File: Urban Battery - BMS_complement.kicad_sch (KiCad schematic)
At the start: 41 parts, among them J1 BMS IO, J10 E-Stop, J11 Contactor Connector, J12 Thermistor, J13 Thermistor, J14 Thermistor, J2 OLED Header, J3 CAN, J4 CAN, J5 Charge Connector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

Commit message: updated component datasheets
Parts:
- U1: value MCP2515-xSO -> MCP2515-I/SO
- U2: value MCP2551-I-SN -> MCP2561/2
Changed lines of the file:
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@@
       (effects (font (size 1.27 1.27)) (justify left))
     )
-    (property "Value" "MCP2551-I-SN" (id 1) (at 132.8294 212.09 0)
+    (property "Value" "MCP2561/2" (id 1) (at 132.8294 212.09 0)
       (effects (font (size 1.27 1.27)) (justify left))
     )
@@
       (effects (font (size 1.27 1.27) italic) hide)
     )
-    (property "Datasheet" "http://ww1.microchip.com/downloads/en/devicedoc/21667d.pdf" (id 3) (at 130.81 222.25 0)
+    (property "Datasheet" "https://ww1.microchip.com/downloads/en/DeviceDoc/20005167C.pdf" (id 3) (at 130.81 222.25 0)
       (effects (font (size 1.27 1.27)) hide)
     )
@@
       (effects (font (size 1.27 1.27)) hide)
     )
-    (property "Datasheet" "~" (id 3) (at 260.35 144.78 0)
+    (property "Datasheet" "https://www.molex.com/pdm_docs/sd/436500200_sd.pdf" (id 3) (at 260.35 144.78 0)
       (effects (font (size 1.27 1.27)) hide)
     )
@@
       (effects (font (size 1.27 1.27)) (justify left))
     )
-    (property "Value" "MCP2515-xSO" (id 1) (at 78.2194 209.55 0)
+    (property "Value" "MCP2515-I/SO" (id 1) (at 78.2194 209.55 0)
       (effects (font (size 1.27 1.27)) (justify left))
     )
@@
       (effects (font (size 1.27 1.27) italic) hide)
     )
-    (property "Datasheet" "http://ww1.microchip.com/downloads/en/DeviceDoc/21801e.pdf" (id 3) (at 78.74 250.19 0)
+    (property "Datasheet" "https://ww1.microchip.com/downloads/en/DeviceDoc/MCP2515-Stand-Alone-CAN-Controller-with-SPI-20001801J.pdf" (id 3) (at 78.74 250.19 0)
       (effects (font (size 1.27 1.27)) hide)
     )
@@
       (effects (font (size 1.27 1.27)) hide)
     )
-    (property "Datasheet" "~" (id 3) (at 256.54 58.42 0)
+    (property "Datasheet" "https://www.molex.com/pdm_docs/sd/436500200_sd.pdf" (id 3) (at 256.54 58.42 0)
       (effects (font (size 1.27 1.27)) hide)
     )
@@
       (effects (font (size 1.27 1.27)) hide)
     )
-    (property "Datasheet" "~" (id 3) (at 261.62 191.77 0)
+    (property "Datasheet" "https://www.digikey.ca/en/products/detail/phoenix-contact/1729128/260615?utm_adgroup=Connectors%2C%20Interconnects&utm_source=google&utm_medium=cpc&utm_campaign=Shopping_Supplier_Phoenix%20Contact_0277_Co-op&utm_term=&productid=260615&gclid=CjwKCAiAhqCdBhB0EiwAH8M_GunPOPKCx2ICSjHcvsaLY6vUI2QZJvTEruKzXstBsW3mdooGzr9-MRoCGRIQAvD_BwE" (id 3) (at 261.62 191.77 0)
       (effects (font (size 1.27 1.27)) hide)
     )
@@
       (effects (font (size 1.27 1.27)) hide)
     )
-    (property "Datasheet" "~" (id 3) (at 260.35 151.13 0)
+    (property "Datasheet" "https://www.molex.com/pdm_docs/sd/436500200_sd.pdf" (id 3) (at 260.35 151.13 0)
       (effects (font (size 1.27 1.27)) hide)
     )
@@
       (effects (font (size 1.27 1.27)) hide)
     )
-    (property "Datasheet" "~" (id 3) (at 260.35 157.48 0)
+    (property "Datasheet" "https://www.molex.com/pdm_docs/sd/436500200_sd.pdf" (id 3) (at 260.35 157.48 0)
       (effects (font (size 1.27 1.27)) hide)
     )
@@
       (effects (font (size 1.27 1.27)) hide)
     )
-    (property "Datasheet" "~" (id 3) (at 261.62 123.19 0)
+    (property "Datasheet" "https://www.digikey.ca/en/products/detail/phoenix-contact/1729128/260615?utm_adgroup=Connectors%2C%20Interconnects&utm_source=google&utm_medium=cpc&utm_campaign=Shopping_Supplier_Phoenix%20Contact_0277_Co-op&utm_term=&productid=260615&gclid=CjwKCAiAhqCdBhB0EiwAH8M_GunPOPKCx2ICSjHcvsaLY6vUI2QZJvTEruKzXstBsW3mdooGzr9-MRoCGRIQAvD_BwE" (id 3) (at 261.62 123.19 0)
       (effects (font (size 1.27 1.27)) hide)
     )
@@
       (effects (font (size 1.27 1.27)) hide)
     )
-    (property "Datasheet" "~" (id 3) (at 261.62 185.42 0)
+    (property "Datasheet" "https://www.digikey.ca/en/products/detail/phoenix-contact/1729128/260615?utm_adgroup=Connectors%2C%20Interconnects&utm_source=google&utm_medium=cpc&utm_campaign=Shopping_Supplier_Phoenix%20Contact_0277_Co-op&utm_term=&productid=260615&gclid=CjwKCAiAhqCdBhB0EiwAH8M_GunPOPKCx2ICSjHcvsaLY6vUI2QZJvTEruKzXstBsW3mdooGzr9-MRoCGRIQAvD_BwE" (id 3) (at 261.62 185.42 0)
       (effects (font (size 1.27 1.27)) hide)
     )
@@
       (effects (font (size 1.27 1.27)) hide)
     )
-    (property "Datasheet" "~" (id 3) (at 260.35 138.43 0)
+    (property "Datasheet" "https://www.molex.com/pdm_docs/sd/436500200_sd.pdf" (id 3) (at 260.35 138.43 0)
       (effects (font (size 1.27 1.27)) hide)
     )
@@
       (effects (font (size 1.27 1.27)) hide)
     )
-    (property "Datasheet" "~" (id 3) (at 261.62 198.12 0)
+    (property "Datasheet" "https://www.digikey.ca/en/products/detail/phoenix-contact/1729128/260615?utm_adgroup=Connectors%2C%20Interconnects&utm_source=google&utm_medium=cpc&utm_campaign=Shopping_Supplier_Phoenix%20Contact_0277_Co-op&utm_term=&productid=260615&gclid=CjwKCAiAhqCdBhB0EiwAH8M_GunPOPKCx2ICSjHcvsaLY6vUI2QZJvTEruKzXstBsW3mdooGzr9-MRoCGRIQAvD_BwE" (id 3) (at 261.62 198.12 0)
       (effects (font (size 1.27 1.27)) hide)
     )
@@
     )
     (path "/38a517b7-e3ff-44bb-944f-e8a6ce592fe9"
-      (reference "U1") (unit 1) (value "MCP2515-xSO") (footprint "Package_SO:SOIC-18W_7.5x11.6mm_P1.27mm")
+      (reference "U1") (unit 1) (value "MCP2515-I/SO") (footprint "Package_SO:SOIC-18W_7.5x11.6mm_P1.27mm")
     )
     (path "/1697370a-3628-470c-bc0f-a1855dcdcce5"
-      (reference "U2") (unit 1) (value "MCP2551-I-SN") (footprint "Package_SO:SOIC-8_3.9x4.9mm_P1.27mm")
+      (reference "U2") (unit 1) (value "MCP2561/2") (footprint "Package_SO:SOIC-8_3.9x4.9mm_P1.27mm")
     )
     (path "/3df7eced-ac2b-49df-aad6-56219ac8510a"

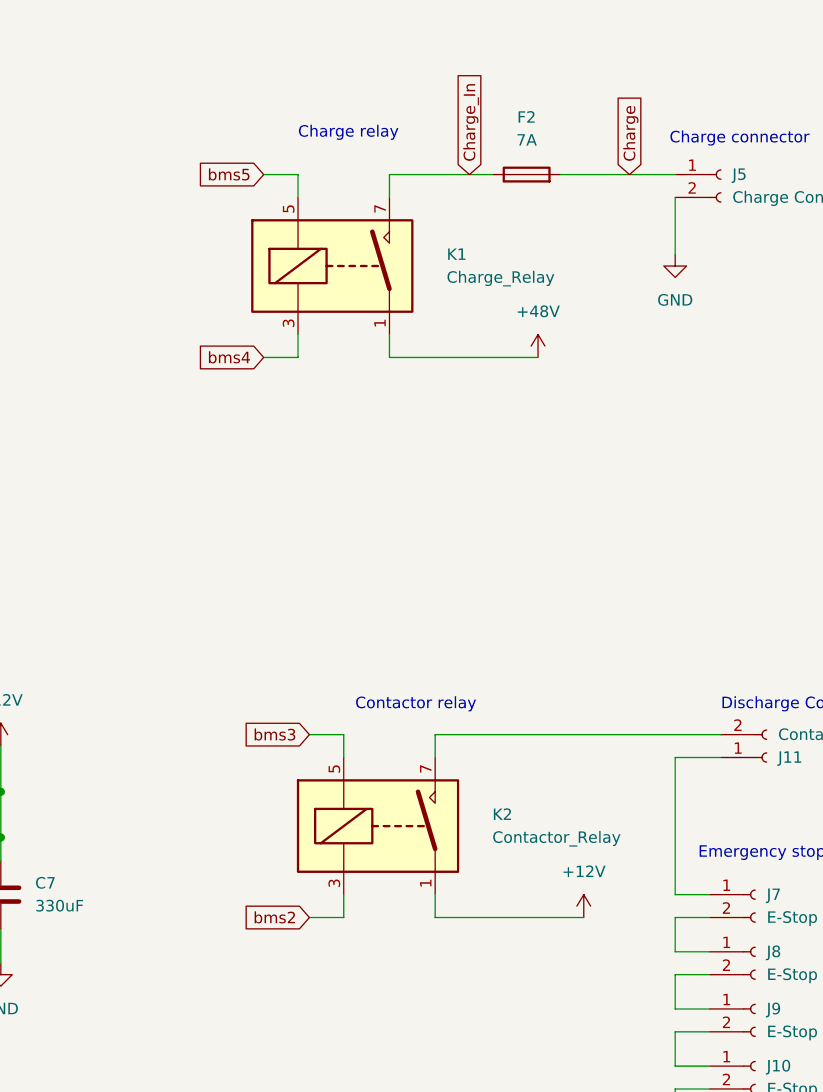
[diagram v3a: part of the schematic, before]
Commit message: Updated relays & silkscreen
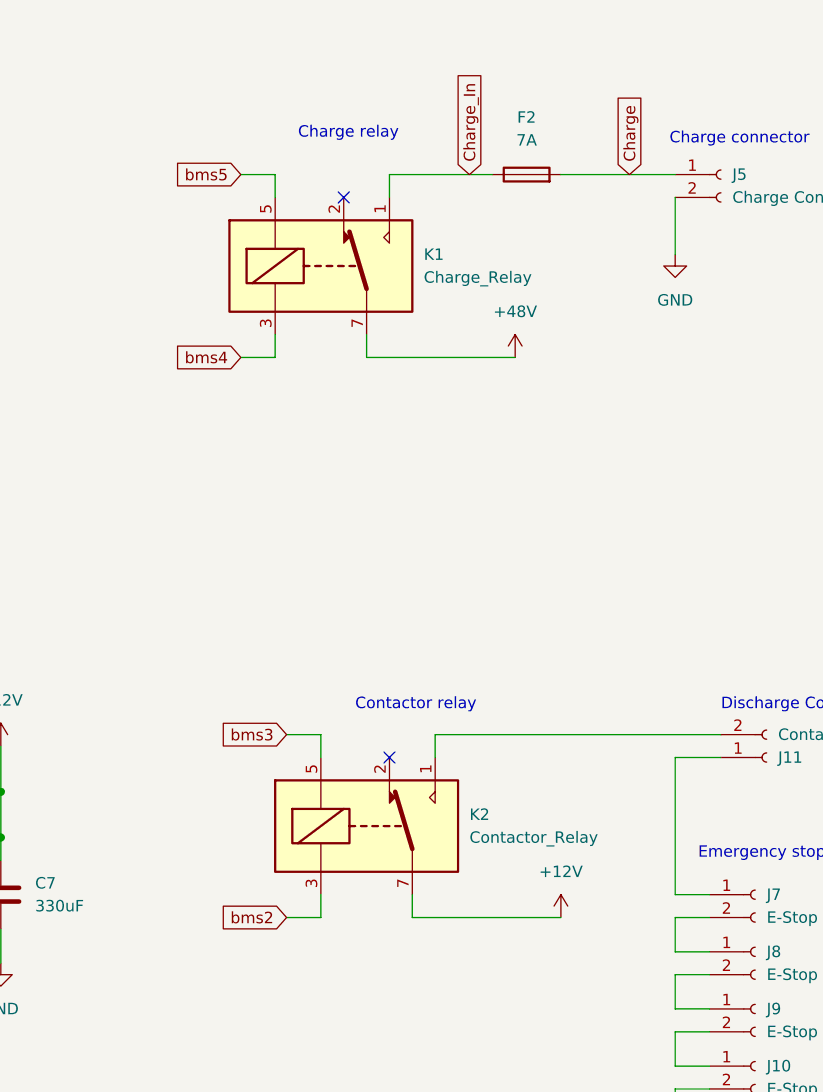
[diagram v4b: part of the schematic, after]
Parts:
- removed K1: Charge_Relay, BMS_Custom_Footprints:Relay_RT334048, symbol Relay:SILxx-1Axx-71x
- removed K2: Contactor_Relay, BMS_Custom_Footprints:Relay_RT334048, symbol Relay:SILxx-1Axx-71x
- added K1: Charge_Relay, BMS_Custom_Footprints:Relay_RT334048, symbol Relay:SILxx-1Cxx-51x
- added K2: Contactor_Relay, BMS_Custom_Footprints:Relay_RT334048, symbol Relay:SILxx-1Cxx-51x
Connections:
- net +12V: now also K2.7
- net +48V: now also K1.7
- net Charge_In: now also K1.1
- net bms2: now also K2.3
- net bms3: now also K2.5
- net bms4: now also K1.3
- net bms5: now also K1.5
- net at J11.2 (Pin_2): now also K2.1
- no-connect marks 32 -> 34
